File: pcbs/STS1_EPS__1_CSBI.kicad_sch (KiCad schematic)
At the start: 2 parts

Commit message: Finished first revision of schematic.
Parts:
- CSBI_1, CSBI_2: value (none) -> ~; footprint (none) -> Connector_PinHeader_2.00mm:PinHeader_2x25_P2.00mm_Vertical
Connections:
- net EPS_BAT_GOOD: no longer names the net of CSBI_2.21 (Pin_21), CSBI_2.22 (Pin_22)
- net VOUT: no longer names the net of CSBI_1.5 (Pin_5), CSBI_1.6 (Pin_6), CSBI_1.7 (Pin_7), CSBI_1.8 (Pin_8)
- net VOUT: no longer CSBI_2.43 (Pin_43), CSBI_2.44 (Pin_44), CSBI_2.45 (Pin_45), CSBI_2.46 (Pin_46)
- new net: CSBI_2.43 (Pin_43), CSBI_2.44 (Pin_44), CSBI_2.45 (Pin_45), CSBI_2.46 (Pin_46)
- no-connect marks 15 -> 18
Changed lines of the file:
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@@
   (junction (at 87.63 105.41) (diameter 0) (color 0 0 0 0)
+  )
+  (junction (at 165.1 58.42) (diameter 0) (color 0 0 0 0)
   )
   (junction (at 87.63 85.09) (diameter 0) (color 0 0 0 0)
@@
   (no_connect (at 87.63 80.01))
   (no_connect (at 87.63 77.47))
+  (no_connect (at 165.1 68.58))
   (no_connect (at 165.1 55.88))
   (no_connect (at 87.63 74.93))
@@
   (no_connect (at 87.63 87.63))
   (no_connect (at 139.7 53.34))
+  (no_connect (at 154.94 96.52))
   (no_connect (at 165.1 71.12))
   (no_connect (at 177.8 71.12))
+  (no_connect (at 80.01 49.53))
   (bus_entry (at 149.86 93.98) (size 2.54 -2.54)
     (stroke (width 0) (type default) (color 0 0 0 0))
@@
   )
   (wire (pts (xy 165.1 91.44) (xy 152.4 91.44))
+    (stroke (width 0) (type default) (color 0 0 0 0))
+  )
+  (wire (pts (xy 161.29 58.42) (xy 165.1 58.42))
     (stroke (width 0) (type default) (color 0 0 0 0))
   )
@@
     (effects (font (size 1.27 1.27)) (justify left bottom))
   )
-  (hierarchical_label "VOUT" (shape input) (at 154.94 96.52 180)
-    (effects (font (size 1.27 1.27)) (justify right))
-  )
-  (hierarchical_label "VOUT" (shape input) (at 80.01 49.53 180)
+  (hierarchical_label "EPS_BAT_FAULT" (shape input) (at 161.29 58.42 180)
     (effects (font (size 1.27 1.27)) (justify right))
   )
@@
     (effects (font (size 1.27 1.27)) (justify right))
   )
-  (hierarchical_label "EPS_BAT_GOOD" (shape input) (at 165.1 68.58 180)
-    (effects (font (size 1.27 1.27)) (justify right))
-  )
-  (hierarchical_label "EPS_BAT_FAULT" (shape input) (at 165.1 58.42 180)
-    (effects (font (size 1.27 1.27)) (justify right))
-  )
   (symbol (lib_id "Connector_Generic:Conn_02x25_Odd_Even") (at 92.71 74.93 0) (unit 1)
     (in_bom yes) (on_board yes)
     (property "Reference" "CSBI_1" (id 0) (at 93.98 38.9382 0))
-    (property "Value" "" (id 1) (at 93.98 41.2496 0))
-    (property "Footprint" "" (id 2) (at 92.71 74.93 0)
+    (property "Value" "~" (id 1) (at 93.98 41.2496 0))
+    (property "Footprint" "Connector_PinHeader_2.00mm:PinHeader_2x25_P2.00mm_Vertical" (id 2) (at 92.71 74.93 0)
       (effects (font (size 1.27 1.27)) hide)
     )
@@
     (in_bom yes) (on_board yes)
     (property "Reference" "CSBI_2" (id 0) (at 171.45 37.6682 0))
-    (property "Value" "" (id 1) (at 171.45 39.9796 0))
-    (property "Footprint" "" (id 2) (at 170.18 73.66 0)
+    (property "Value" "~" (id 1) (at 171.45 39.9796 0))
+    (property "Footprint" "Connector_PinHeader_2.00mm:PinHeader_2x25_P2.00mm_Vertical" (id 2) (at 170.18 73.66 0)
       (effects (font (size 1.27 1.27)) hide)
     )
@@
       (effects (font (size 1.27 1.27)) hide)
     )
-    (property "Value" "" (id 1) (at 84.3788 44.577 90)
+    (property "Value" "~" (id 1) (at 84.3788 44.577 90)
       (effects (font (size 1.27 1.27)) (justify right))
     )
@@
       (effects (font (size 1.27 1.27)) hide)
     )
-    (property "Value" "" (id 1) (at 84.3788 47.117 90)
+    (property "Value" "~" (id 1) (at 84.3788 47.117 90)
       (effects (font (size 1.27 1.27)) (justify right))
     )
@@
       (effects (font (size 1.27 1.27)) hide)
     )
-    (property "Value" "" (id 1) (at 84.3788 54.737 90)
+    (property "Value" "~" (id 1) (at 84.3788 54.737 90)
       (effects (font (size 1.27 1.27)) (justify right))
     )
@@
       (effects (font (size 1.27 1.27)) hide)
     )
-    (property "Value" "" (id 1) (at 84.3788 85.217 90)
+    (property "Value" "~" (id 1) (at 84.3788 85.217 90)
       (effects (font (size 1.27 1.27)) (justify right))
     )
@@
       (effects (font (size 1.27 1.27)) hide)
     )
-    (property "Value" "" (id 1) (at 84.3788 102.997 90)
+    (property "Value" "~" (id 1) (at 84.3788 102.997 90)
       (effects (font (size 1.27 1.27)) (justify right))
     )
@@
       (effects (font (size 1.27 1.27)) hide)
     )
-    (property "Value" "" (id 1) (at 84.3788 105.537 90)
+    (property "Value" "~" (id 1) (at 84.3788 105.537 90)
       (effects (font (size 1.27 1.27)) (justify right))
     )
@@
       (effects (font (size 1.27 1.27)) hide)
     )
-    (property "Value" "" (id 1) (at 161.8488 43.307 90)
+    (property "Value" "~" (id 1) (at 161.8488 43.307 90)
       (effects (font (size 1.27 1.27)) (justify right))
     )
@@
       (effects (font (size 1.27 1.27)) hide)
     )
-    (property "Value" "" (id 1) (at 161.8488 45.847 90)
+    (property "Value" "~" (id 1) (at 161.8488 45.847 90)
       (effects (font (size 1.27 1.27)) (justify right))
     )
@@
       (effects (font (size 1.27 1.27)) hide)
     )
-    (property "Value" "" (id 1) (at 161.8488 104.267 90)
+    (property "Value" "~" (id 1) (at 161.8488 104.267 90)
       (effects (font (size 1.27 1.27)) (justify right))
     )
@@
       (effects (font (size 1.27 1.27)) hide)
     )
-    (property "Value" "" (id 1) (at 161.8488 101.727 90)
+    (property "Value" "~" (id 1) (at 161.8488 101.727 90)
       (effects (font (size 1.27 1.27)) (justify right))
     )
@@
       (effects (font (size 1.27 1.27)) hide)
     )
-    (property "Value" "" (id 1) (at 161.8488 76.327 90)
+    (property "Value" "~" (id 1) (at 161.8488 76.327 90)
       (effects (font (size 1.27 1.27)) (justify right))
     )
@@
       (effects (font (size 1.27 1.27)) hide)
     )
-    (property "Value" "" (id 1) (at 161.8488 63.627 90)
+    (property "Value" "~" (id 1) (at 161.8488 63.627 90)
       (effects (font (size 1.27 1.27)) (justify right))
     )
@@
       (effects (font (size 1.27 1.27)) hide)
     )
-    (property "Value" "" (id 1) (at 161.8488 94.107 90)
+    (property "Value" "~" (id 1) (at 161.8488 94.107 90)
       (effects (font (size 1.27 1.27)) (justify right))
     )
@@
       (effects (font (size 1.27 1.27)) hide)
     )
-    (property "Value" "" (id 1) (at 84.3788 72.517 90)
+    (property "Value" "~" (id 1) (at 84.3788 72.517 90)
       (effects (font (size 1.27 1.27)) (justify right))
     )
@@
       (effects (font (size 1.27 1.27)) hide)
     )
-    (property "Value" "" (id 1) (at 84.3788 95.377 90)
+    (property "Value" "~" (id 1) (at 84.3788 95.377 90)
       (effects (font (size 1.27 1.27)) (justify right))
     )
@@
       (effects (font (size 1.27 1.27)) hide)
     )
-    (property "Value" "" (id 1) (at 161.8488 53.467 90)
-      (effects (font (size 1.27 1.27)) (justify right))
-    )
+    (property "Value" "~" (id 1) (at 161.8488 53.467 90)
+      (effects (font (size 1.27 1.27)) (justify right))
+    )

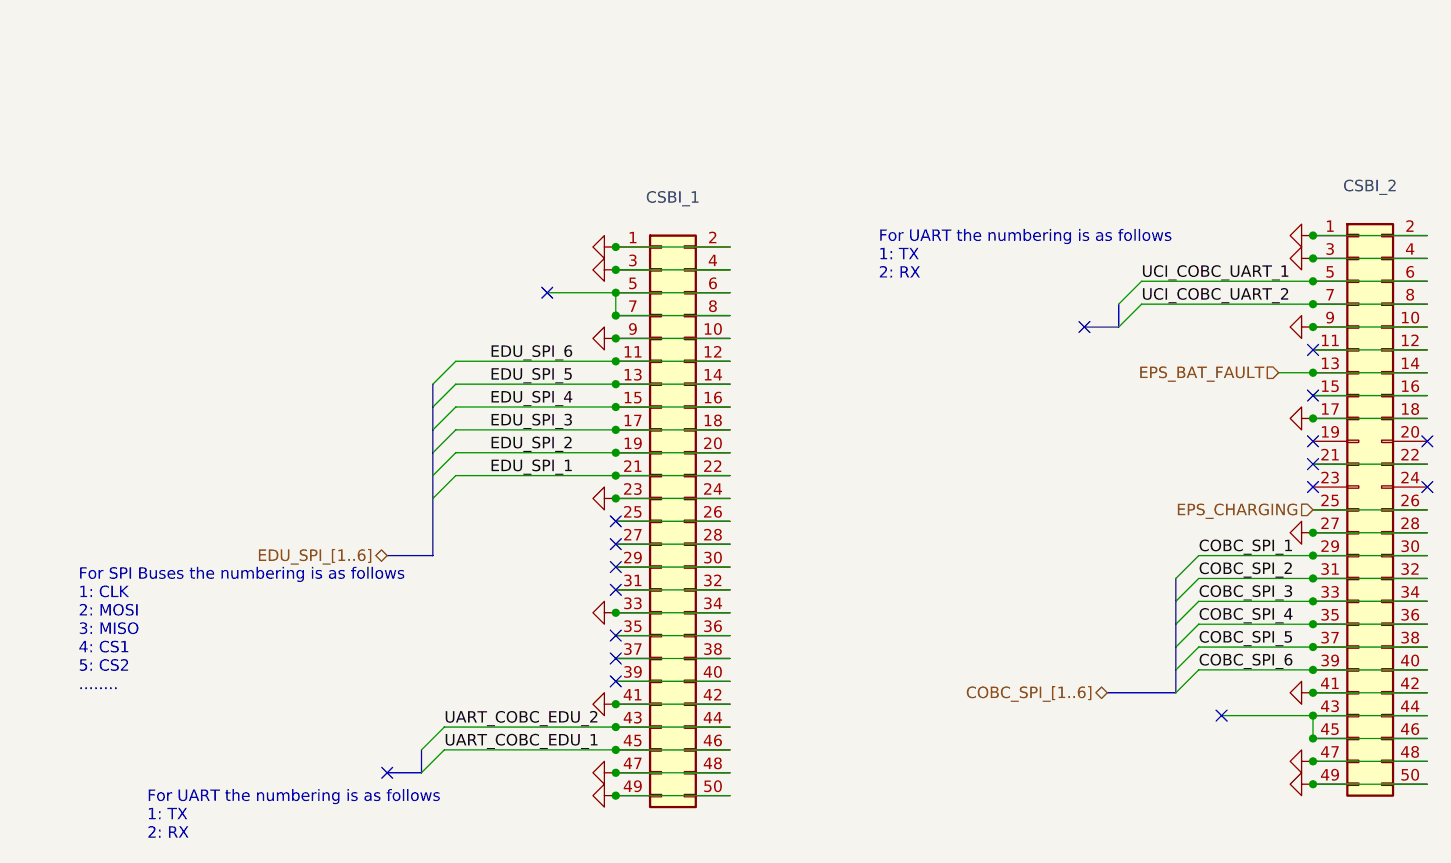
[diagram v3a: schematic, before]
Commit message: Cleared all DRC errors of STS1_EPS_1.
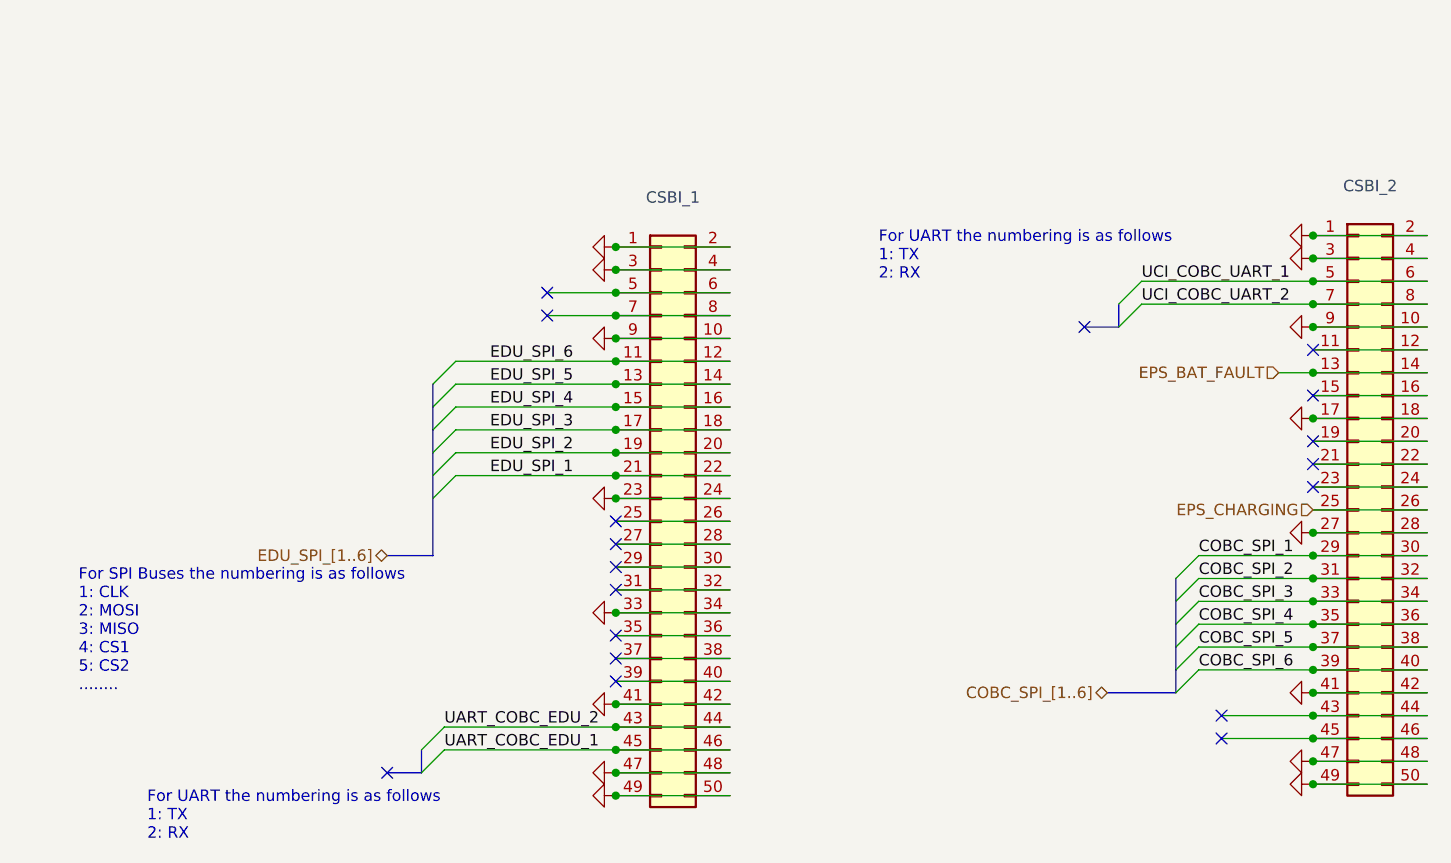
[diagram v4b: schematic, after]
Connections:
- net at CSBI_1.5 (Pin_5), CSBI_1.6 (Pin_6): no longer CSBI_1.7 (Pin_7), CSBI_1.8 (Pin_8)
- net at CSBI_2.19 (Pin_19): now also CSBI_2.20 (Pin_20)
- net at CSBI_2.23 (Pin_23): now also CSBI_2.24 (Pin_24)
- net at CSBI_2.43 (Pin_43), CSBI_2.44 (Pin_44): no longer CSBI_2.45 (Pin_45), CSBI_2.46 (Pin_46)
- new net: CSBI_1.7 (Pin_7), CSBI_1.8 (Pin_8)
- new net: CSBI_2.45 (Pin_45), CSBI_2.46 (Pin_46)
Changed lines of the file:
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@@
   (junction (at 87.63 102.87) (diameter 0) (color 0 0 0 0)
   )
+  (junction (at 87.63 52.07) (diameter 0) (color 0 0 0 0)
+  )
   (junction (at 87.63 97.79) (diameter 0) (color 0 0 0 0)
   )
@@
   (junction (at 165.1 76.2) (diameter 0) (color 0 0 0 0)
   )
-  (junction (at 87.63 52.07) (diameter 0) (color 0 0 0 0)
-  )
   (junction (at 87.63 105.41) (diameter 0) (color 0 0 0 0)
   )
@@
   (junction (at 87.63 85.09) (diameter 0) (color 0 0 0 0)
   )
+  (junction (at 165.1 99.06) (diameter 0) (color 0 0 0 0)
+  )
   (junction (at 165.1 88.9) (diameter 0) (color 0 0 0 0)
   )
@@
   )
   (junction (at 87.63 54.61) (diameter 0) (color 0 0 0 0)
-  )
-  (junction (at 165.1 99.06) (diameter 0) (color 0 0 0 0)
   )
   (junction (at 165.1 96.52) (diameter 0) (color 0 0 0 0)
@@
   (no_connect (at 165.1 68.58))
   (no_connect (at 165.1 55.88))
+  (no_connect (at 80.01 52.07))
   (no_connect (at 87.63 74.93))
-  (no_connect (at 177.8 66.04))
+  (no_connect (at 154.94 99.06))
   (no_connect (at 87.63 82.55))
   (no_connect (at 165.1 60.96))
@@
   (no_connect (at 154.94 96.52))
   (no_connect (at 165.1 71.12))
-  (no_connect (at 177.8 71.12))
   (no_connect (at 80.01 49.53))
   (bus_entry (at 149.86 93.98) (size 2.54 -2.54)
@@
     (stroke (width 0) (type default) (color 0 0 0 0))
   )
-  (wire (pts (xy 165.1 96.52) (xy 165.1 99.06))
-    (stroke (width 0) (type default) (color 0 0 0 0))
-  )
   (wire (pts (xy 87.63 97.79) (xy 100.33 97.79))
     (stroke (width 0) (type default) (color 0 0 0 0))
@@
     (stroke (width 0) (type default) (color 0 0 0 0))
   )
+  (wire (pts (xy 165.1 71.12) (xy 177.8 71.12))
+    (stroke (width 0) (type default) (color 0 0 0 0))
+  )
   (bus (pts (xy 67.31 72.39) (xy 67.31 78.74))
     (stroke (width 0) (type default) (color 0 0 0 0))
@@
     (stroke (width 0) (type default) (color 0 0 0 0))
   )
+  (wire (pts (xy 165.1 86.36) (xy 152.4 86.36))
+    (stroke (width 0) (type default) (color 0 0 0 0))
+  )
+  (wire (pts (xy 165.1 63.5) (xy 177.8 63.5))
+    (stroke (width 0) (type default) (color 0 0 0 0))
+  )
+  (wire (pts (xy 87.63 90.17) (xy 100.33 90.17))
+    (stroke (width 0) (type default) (color 0 0 0 0))
+  )
+  (wire (pts (xy 87.63 92.71) (xy 100.33 92.71))
+    (stroke (width 0) (type default) (color 0 0 0 0))
+  )
+  (wire (pts (xy 165.1 55.88) (xy 177.8 55.88))
+    (stroke (width 0) (type default) (color 0 0 0 0))
+  )
+  (wire (pts (xy 87.63 77.47) (xy 100.33 77.47))
+    (stroke (width 0) (type default) (color 0 0 0 0))
+  )
+  (bus (pts (xy 149.86 86.36) (xy 149.86 88.9))
+    (stroke (width 0) (type default) (color 0 0 0 0))
+  )
+  (bus (pts (xy 143.51 50.8) (xy 143.51 53.34))
+    (stroke (width 0) (type default) (color 0 0 0 0))
+  )
+  (wire (pts (xy 165.1 76.2) (xy 177.8 76.2))
+    (stroke (width 0) (type default) (color 0 0 0 0))
+  )
+  (wire (pts (xy 87.63 62.23) (xy 100.33 62.23))
+    (stroke (width 0) (type default) (color 0 0 0 0))
+  )
+  (wire (pts (xy 68.58 97.79) (xy 87.63 97.79))
+    (stroke (width 0) (type default) (color 0 0 0 0))
+  )
+  (wire (pts (xy 154.94 99.06) (xy 165.1 99.06))
+    (stroke (width 0) (type default) (color 0 0 0 0))
+  )
   (wire (pts (xy 165.1 99.06) (xy 177.8 99.06))
     (stroke (width 0) (type default) (color 0 0 0 0))
   )
-  (wire (pts (xy 165.1 86.36) (xy 152.4 86.36))
-    (stroke (width 0) (type default) (color 0 0 0 0))
-  )
-  (wire (pts (xy 165.1 63.5) (xy 177.8 63.5))
-    (stroke (width 0) (type default) (color 0 0 0 0))
-  )
-  (wire (pts (xy 87.63 90.17) (xy 100.33 90.17))
-    (stroke (width 0) (type default) (color 0 0 0 0))
-  )
-  (wire (pts (xy 87.63 92.71) (xy 100.33 92.71))
-    (stroke (width 0) (type default) (color 0 0 0 0))
-  )
-  (wire (pts (xy 165.1 55.88) (xy 177.8 55.88))
-    (stroke (width 0) (type default) (color 0 0 0 0))
-  )
-  (wire (pts (xy 87.63 77.47) (xy 100.33 77.47))
-    (stroke (width 0) (type default) (color 0 0 0 0))
-  )
-  (bus (pts (xy 149.86 86.36) (xy 149.86 88.9))
-    (stroke (width 0) (type default) (color 0 0 0 0))
-  )
-  (bus (pts (xy 143.51 50.8) (xy 143.51 53.34))
-    (stroke (width 0) (type default) (color 0 0 0 0))
-  )
-  (wire (pts (xy 165.1 76.2) (xy 177.8 76.2))
-    (stroke (width 0) (type default) (color 0 0 0 0))
-  )
-  (wire (pts (xy 87.63 62.23) (xy 100.33 62.23))
-    (stroke (width 0) (type default) (color 0 0 0 0))
-  )
-  (wire (pts (xy 68.58 97.79) (xy 87.63 97.79))
-    (stroke (width 0) (type default) (color 0 0 0 0))
-  )
   (wire (pts (xy 87.63 87.63) (xy 100.33 87.63))
     (stroke (width 0) (type default) (color 0 0 0 0))
@@
     (stroke (width 0) (type default) (color 0 0 0 0))
   )
-  (wire (pts (xy 87.63 49.53) (xy 87.63 52.07))
-    (stroke (width 0) (type default) (color 0 0 0 0))
-  )
   (wire (pts (xy 165.1 96.52) (xy 177.8 96.52))
     (stroke (width 0) (type default) (color 0 0 0 0))
@@
     (stroke (width 0) (type default) (color 0 0 0 0))
   )
+  (wire (pts (xy 165.1 66.04) (xy 177.8 66.04))
+    (stroke (width 0) (type default) (color 0 0 0 0))
+  )
   (bus (pts (xy 67.31 78.74) (xy 62.23 78.74))
     (stroke (width 0) (type default) (color 0 0 0 0))
@@
     (stroke (width 0) (type default) (color 0 0 0 0))
   )
+  (wire (pts (xy 80.01 52.07) (xy 87.63 52.07))
+    (stroke (width 0) (type default) (color 0 0 0 0))
+  )

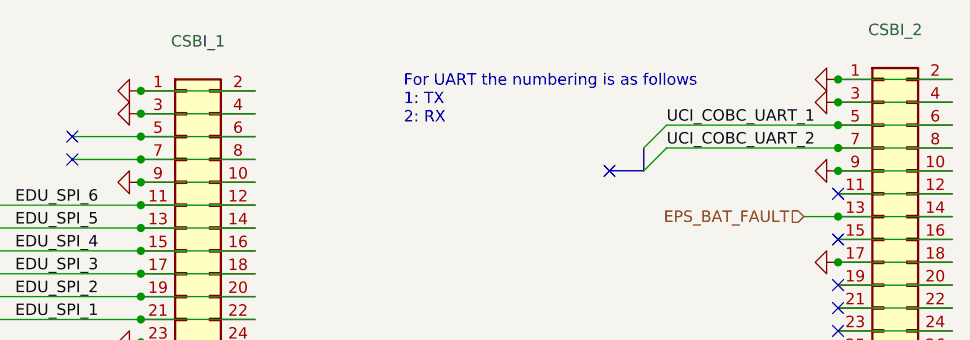
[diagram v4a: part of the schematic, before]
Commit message: Added part numbers to some of the components. No functional changes.
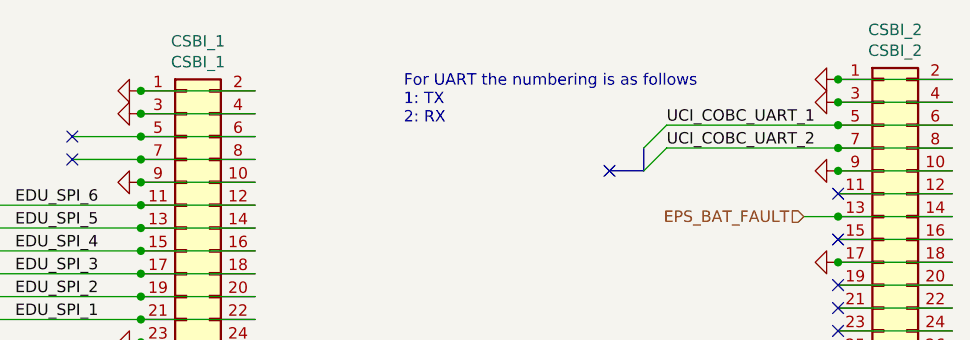
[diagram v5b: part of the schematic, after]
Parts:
- CSBI_1: value ~ -> CSBI_1; Part# (none) -> ESQT-125-02-F-D-800
- CSBI_2: value ~ -> CSBI_2; Part# (none) -> ESQT-125-02-F-D-800
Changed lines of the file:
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@@
     (in_bom yes) (on_board yes)
     (property "Reference" "CSBI_1" (id 0) (at 93.98 38.9382 0))
-    (property "Value" "~" (id 1) (at 93.98 41.2496 0))
+    (property "Value" "CSBI_1" (id 1) (at 93.98 41.2496 0))
     (property "Footprint" "Connector_PinHeader_2.00mm:PinHeader_2x25_P2.00mm_Vertical" (id 2) (at 92.71 74.93 0)
       (effects (font (size 1.27 1.27)) hide)
     )
     (property "Datasheet" "~" (id 3) (at 92.71 74.93 0)
+      (effects (font (size 1.27 1.27)) hide)
+    )
+    (property "Part#" "ESQT-125-02-F-D-800" (id 4) (at 92.71 74.93 0)
       (effects (font (size 1.27 1.27)) hide)
     )
@@
     (in_bom yes) (on_board yes)
     (property "Reference" "CSBI_2" (id 0) (at 171.45 37.6682 0))
-    (property "Value" "~" (id 1) (at 171.45 39.9796 0))
+    (property "Value" "CSBI_2" (id 1) (at 171.45 39.9796 0))
     (property "Footprint" "Connector_PinHeader_2.00mm:PinHeader_2x25_P2.00mm_Vertical" (id 2) (at 170.18 73.66 0)
       (effects (font (size 1.27 1.27)) hide)
@@
       (effects (font (size 1.27 1.27)) hide)
     )
+    (property "Part#" "ESQT-125-02-F-D-800" (id 4) (at 170.18 73.66 0)
+      (effects (font (size 1.27 1.27)) hide)
+    )
